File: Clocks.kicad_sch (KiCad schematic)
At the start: 9 parts, among them U3 CDCLVC1106, Y2 O 16,0-JT22CT-A-P-3,3-LF

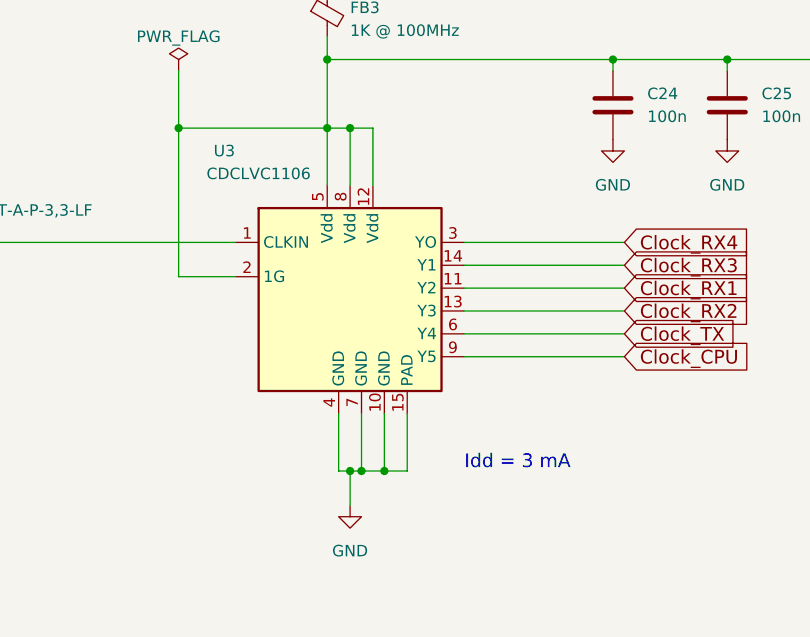
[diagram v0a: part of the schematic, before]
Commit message: Change the clock buffer
Move to one that is temperature rated and has better specs.

Also reroute one clock line to move it from board edge.

Get a list of all parts that aren't rated to at least 105C.

Signed-off-by: Corey Minyard <corey@minyard.net>
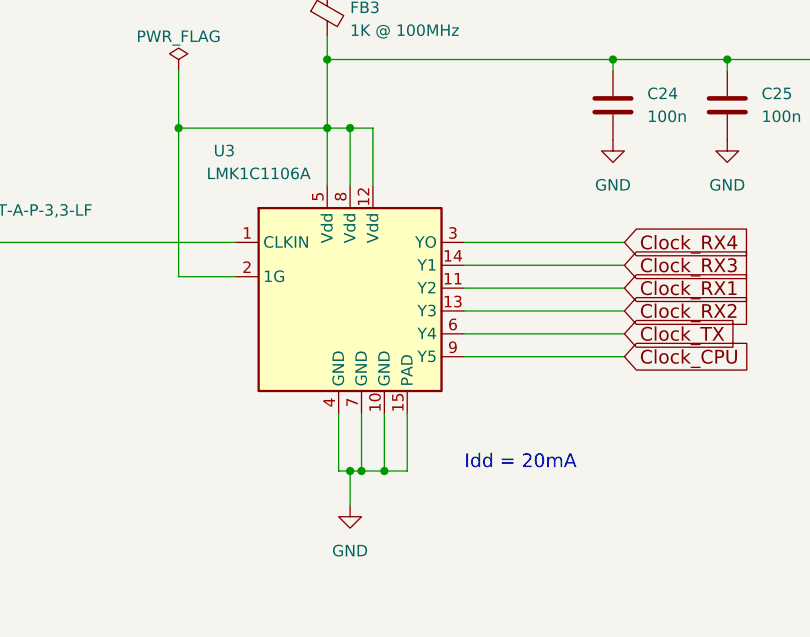
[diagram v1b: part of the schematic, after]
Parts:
- U3: value CDCLVC1106 -> LMK1C1106A; symbol PACSAT_ICs:CDCLVP1106 -> PACSAT_ICs:LMK1C1106A
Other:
- note added: "Idd = 20mA"
- note removed: "Idd = 3 mA"
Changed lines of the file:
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@@
 		)
 	)
-	(text "Idd = 3 mA"
+	(text "Idd = 20mA"
 		(exclude_from_sim no)
 		(at 228.6 132.08 0)
@@
 	)
 	(symbol
-		(lib_id "PACSAT_ICs:CDCLVP1106")
+		(lib_id "PACSAT_ICs:LMK1C1106A")
 		(at 215.9 113.03 0)
 		(unit 1)
@@
 			)
 		)
-		(property "Value" "CDCLVC1106"
+		(property "Value" "LMK1C1106A"
 			(at 205.74 99.06 0)
 			(effects
@@
 					(size 1.27 1.27)
 				)
-			)
-		)
+				(hide yes)
+			)
+		)

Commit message: More work on various things
Signed-off-by: Corey Minyard <corey@minyard.net>
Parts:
- added R56: 33, Resistor_SMD:R_0603_1608Metric_Pad0.98x0.95mm_HandSolder, symbol Device:R
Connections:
- net Clock_CPU: now also R56.2; no longer U3.9 (Y5)
- new net: R56.1, U3.9 (Y5)
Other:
- note added: "AX5043s have capacitive termination at the end of the clocks per their data sheet. Only need series termination on the CPU clock."
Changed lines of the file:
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@@
+		)
+	)
+	(text "AX5043s have capacitive termination\nat the end of the clocks per their\ndata sheet.  Only need series\ntermination on the CPU clock."
+		(exclude_from_sim no)
+		(at 248.412 134.874 0)
+		(effects
+			(font
+				(size 1.524 1.524)
+			)
 		)
 	)
@@
 	(text "Idd = 20mA"
 		(exclude_from_sim no)
-		(at 228.6 132.08 0)
+		(at 195.58 131.826 0)
 		(effects
 			(font
@@
 	(wire
 		(pts
+			(xy 233.68 119.38) (xy 228.6 119.38)
+		)
+		(stroke
+			(width 0)
+			(type default)
+		)
+	)
+	(wire
+		(pts
 			(xy 163.83 106.68) (xy 203.2 106.68)
 		)
@@
 	(wire
 		(pts
+			(xy 242.57 123.19) (xy 246.38 123.19)
+		)
+		(stroke
+			(width 0)
+			(type default)
+		)
+	)
+	(wire
+		(pts
 			(xy 228.6 106.68) (xy 246.38 106.68)
 		)
@@
 	(wire
 		(pts
-			(xy 228.6 119.38) (xy 246.38 119.38)
+			(xy 233.68 123.19) (xy 234.95 123.19)
 		)
 		(stroke
@@
 		(pts
 			(xy 203.2 110.49) (xy 196.85 110.49)
+		)
+		(stroke
+			(width 0)
+			(type default)
+		)
+	)
+	(wire
+		(pts
+			(xy 233.68 123.19) (xy 233.68 119.38)
 		)
 		(stroke
@@
 	(global_label "Clock_CPU"
 		(shape input)
-		(at 246.38 119.38 0)
+		(at 246.38 123.19 0)
 		(fields_autoplaced yes)
 		(effects
@@
 		)
 		(property "Intersheetrefs" "${INTERSHEET_REFS}"
-			(at 261.2237 119.38 0)
+			(at 261.2237 123.19 0)
 			(effects
 				(font
@@
 					(unit 1)
 				)
+			)
+		)
+	)
+	(symbol
+		(lib_id "Device:R")
+		(at 238.76 123.19 90)
+		(unit 1)
+		(exclude_from_sim no)
+		(in_bom yes)
+		(on_board yes)
+		(dnp no)
+		(property "Reference" "R56"
+			(at 241.3 125.73 90)
+			(effects
+				(font
+					(size 1.27 1.27)
+				)
+				(justify left)
+			)
+		)
+		(property "Value" "33"
+			(at 240.538 120.904 90)
+			(effects
+				(font
+					(size 1.27 1.27)
+				)
+				(justify left)
+			)
+		)
+		(property "Footprint" "Resistor_SMD:R_0603_1608Metric_Pad0.98x0.95mm_HandSolder"
+			(at 238.76 124.968 90)
+			(effects
+				(font
+					(size 1.27 1.27)
+				)
+				(hide yes)
+			)
+		)
+		(property "Datasheet" "~"
+			(at 238.76 123.19 0)
+			(effects
+				(font
+					(size 1.27 1.27)
+				)
+			)
+		)
+		(property "Description" ""
+			(at 238.76 123.19 0)
+			(effects
+				(font
+					(size 1.27 1.27)
+				)
+			)
+		)
+		(pin "1"
+		)
+		(pin "2"
+		)
+		(instances
+			(project "PacSat_AFSK"
+				(path "/cc9f42d2-6985-41ac-acab-5ab7b01c5b38/a735fef7-c3fa-4339-b3a6-fbce810c3c4b"
+					(reference "R56")
+					(unit 1)
+				)

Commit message: Change clock and MRAM passives to 0402
Signed-off-by: Corey Minyard <corey@minyard.net>
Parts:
- C23, C24, C25, C26: footprint Capacitor_SMD:C_0603_1608Metric_Pad1.08x0.95mm_HandSolder -> Capacitor_SMD:C_0402_1005Metric_Pad0.74x0.62mm_HandSolder
- R25, R56: footprint Resistor_SMD:R_0603_1608Metric_Pad0.98x0.95mm_HandSolder -> Resistor_SMD:R_0402_1005Metric_Pad0.72x0.64mm_HandSolder
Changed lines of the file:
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@@
 			)
 		)
-		(property "Footprint" "Capacitor_SMD:C_0603_1608Metric_Pad1.08x0.95mm_HandSolder"
+		(property "Footprint" "Capacitor_SMD:C_0402_1005Metric_Pad0.74x0.62mm_HandSolder"
 			(at 246.0752 95.25 0)
 			(effects
@@
 			)
 		)
-		(property "Footprint" "Resistor_SMD:R_0603_1608Metric_Pad0.98x0.95mm_HandSolder"
+		(property "Footprint" "Resistor_SMD:R_0402_1005Metric_Pad0.72x0.64mm_HandSolder"
 			(at 238.76 124.968 90)
 			(effects
@@
 			)
 		)
-		(property "Footprint" "Resistor_SMD:R_0603_1608Metric_Pad0.98x0.95mm_HandSolder"
+		(property "Footprint" "Resistor_SMD:R_0402_1005Metric_Pad0.72x0.64mm_HandSolder"
 			(at 137.922 100.33 90)
 			(effects
@@
 			)
 		)
-		(property "Footprint" "Capacitor_SMD:C_0603_1608Metric_Pad1.08x0.95mm_HandSolder"
+		(property "Footprint" "Capacitor_SMD:C_0402_1005Metric_Pad0.74x0.62mm_HandSolder"
 			(at 126.6952 111.76 0)
 			(effects
@@
 			)
 		)
-		(property "Footprint" "Capacitor_SMD:C_0603_1608Metric_Pad1.08x0.95mm_HandSolder"
+		(property "Footprint" "Capacitor_SMD:C_0402_1005Metric_Pad0.74x0.62mm_HandSolder"
 			(at 258.7752 95.25 0)
 			(effects
@@
 			)
 		)
-		(property "Footprint" "Capacitor_SMD:C_0603_1608Metric_Pad1.08x0.95mm_HandSolder"
+		(property "Footprint" "Capacitor_SMD:C_0402_1005Metric_Pad0.74x0.62mm_HandSolder"
 			(at 271.4752 95.25 0)
 			(effects

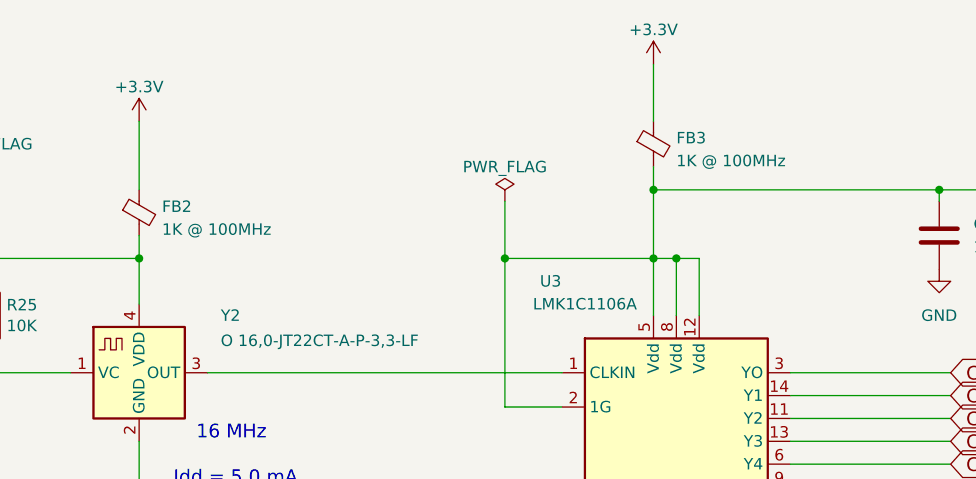
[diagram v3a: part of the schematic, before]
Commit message: More work on components
Signed-off-by: Corey Minyard <corey@minyard.net>
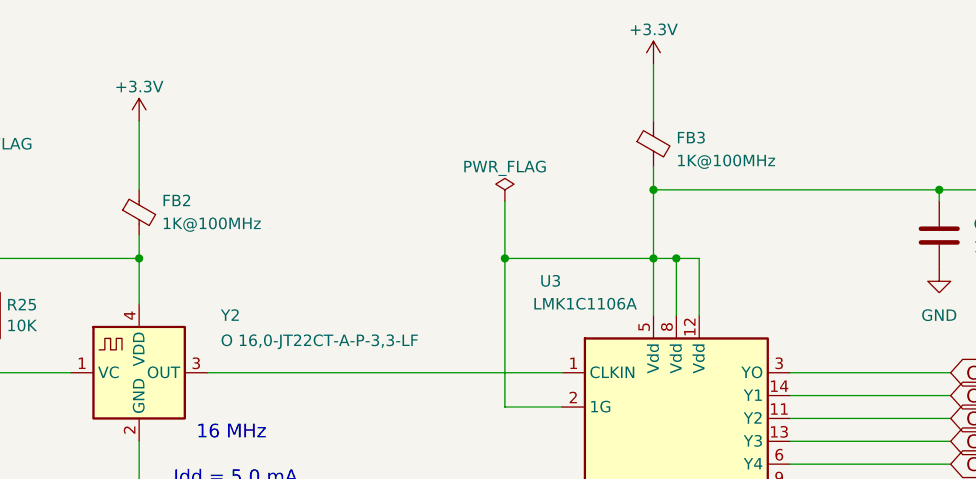
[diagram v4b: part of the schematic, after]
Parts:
- FB2, FB3: value 1K @ 100MHz -> 1K@100MHz
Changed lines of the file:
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@@
 		(fields_autoplaced yes)
 		(property "Reference" "FB2"
-			(at 158.75 88.2269 0)
-			(effects
-				(font
-					(size 1.27 1.27)
-				)
-				(justify left)
-			)
-		)
-		(property "Value" "1K @ 100MHz"
-			(at 158.75 90.7669 0)
+			(at 158.75 87.5918 0)
+			(effects
+				(font
+					(size 1.27 1.27)
+				)
+				(justify left)
+			)
+		)
+		(property "Value" "1K@100MHz"
+			(at 158.75 90.1318 0)
 			(effects
 				(font
@@
 			)
 		)
-		(property "Value" "1K @ 100MHz"
+		(property "Value" "1K@100MHz"
 			(at 215.9 83.1469 0)
 			(effects

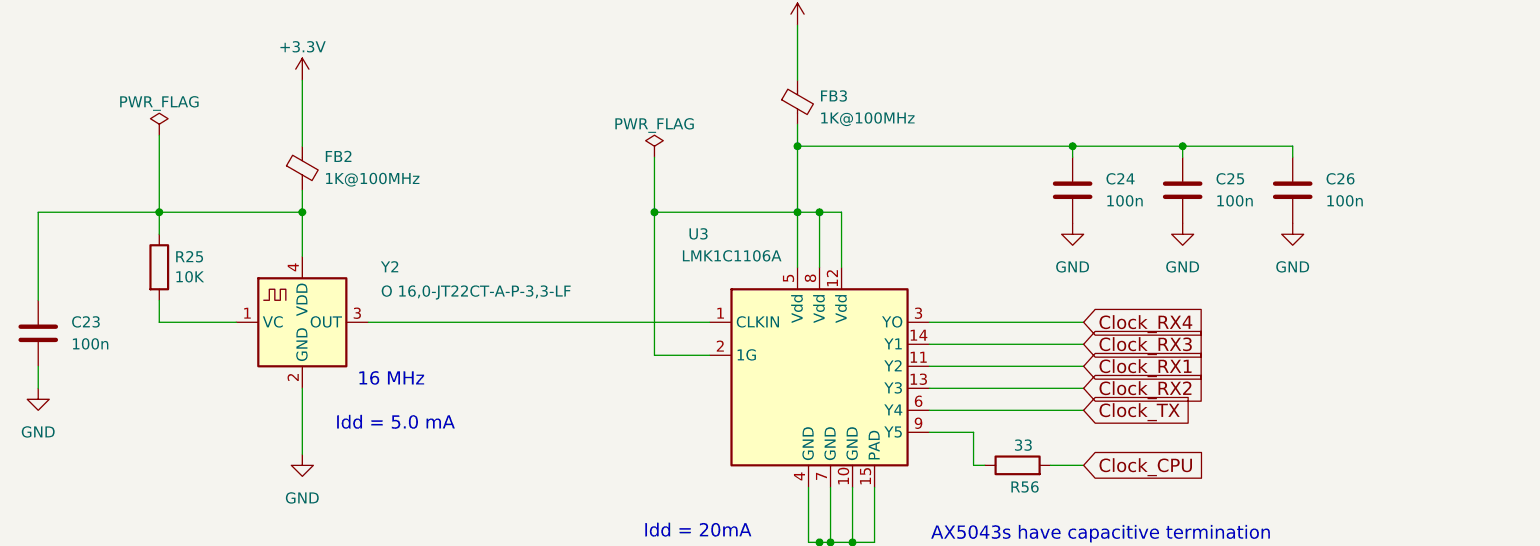
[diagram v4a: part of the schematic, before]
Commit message: Lots of updates to ease manufacturing
Component changes, changes in the formatting of the values, etc.

Signed-off-by: Corey Minyard <corey@minyard.net>
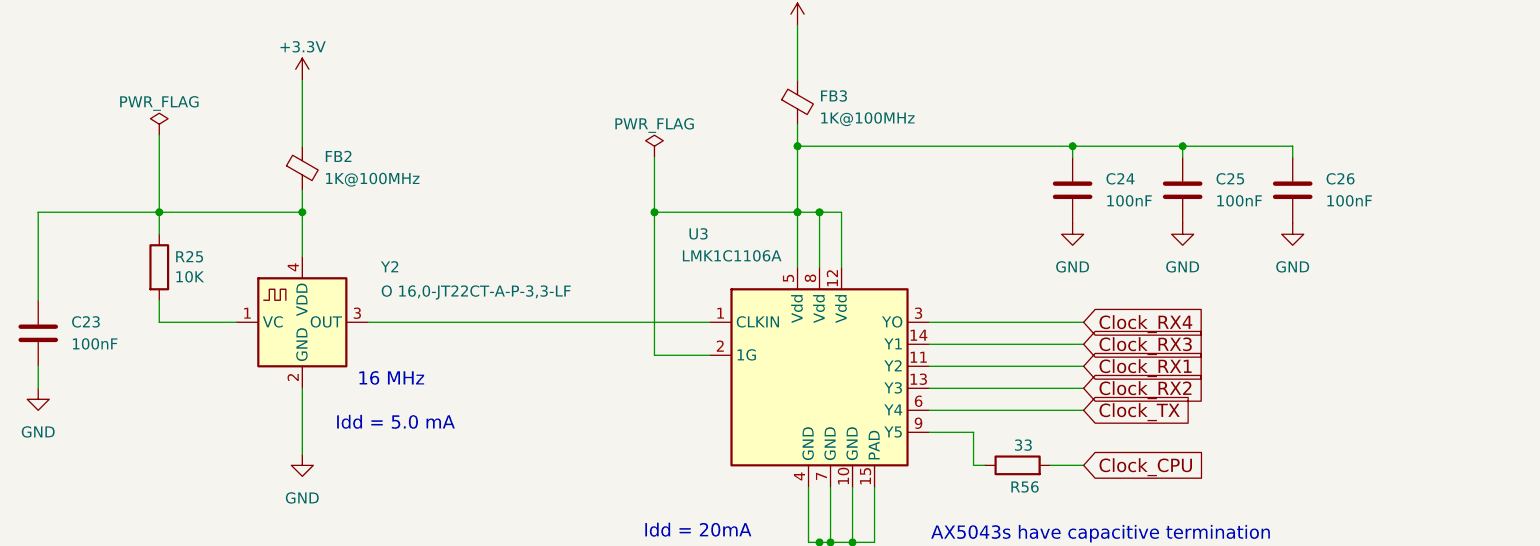
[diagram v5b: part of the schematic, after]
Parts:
- C23, C24, C25, C26: value 100n -> 100nF
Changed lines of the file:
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@@
 			)
 		)
-		(property "Value" "100n"
+		(property "Value" "100nF"
 			(at 248.92 92.7099 0)
 			(effects
@@
 			)
 		)
-		(property "Value" "100n"
+		(property "Value" "100nF"
 			(at 129.54 109.2199 0)
 			(effects
@@
 			)
 		)
-		(property "Value" "100n"
+		(property "Value" "100nF"
 			(at 261.62 92.7099 0)
 			(effects
@@
 			)
 		)
-		(property "Value" "100n"
+		(property "Value" "100nF"
 			(at 274.32 92.7099 0)
 			(effects

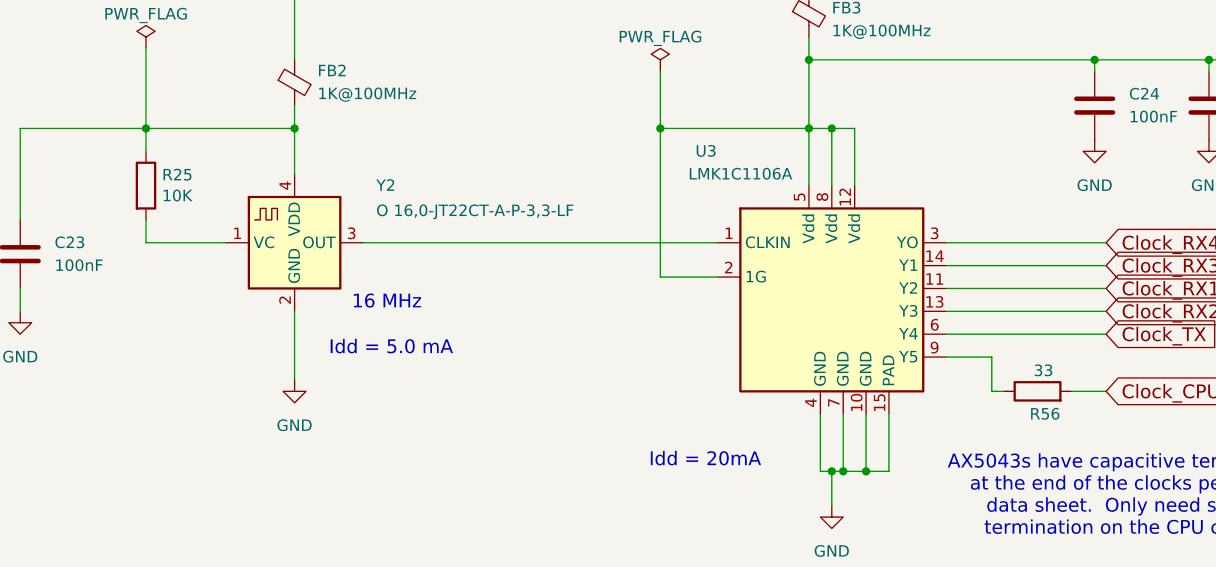
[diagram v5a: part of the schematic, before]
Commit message: Update all resistors to have an ohm symbol
Make it more clean in the BOM what they are.

Signed-off-by: Corey Minyard <corey@minyard.net>
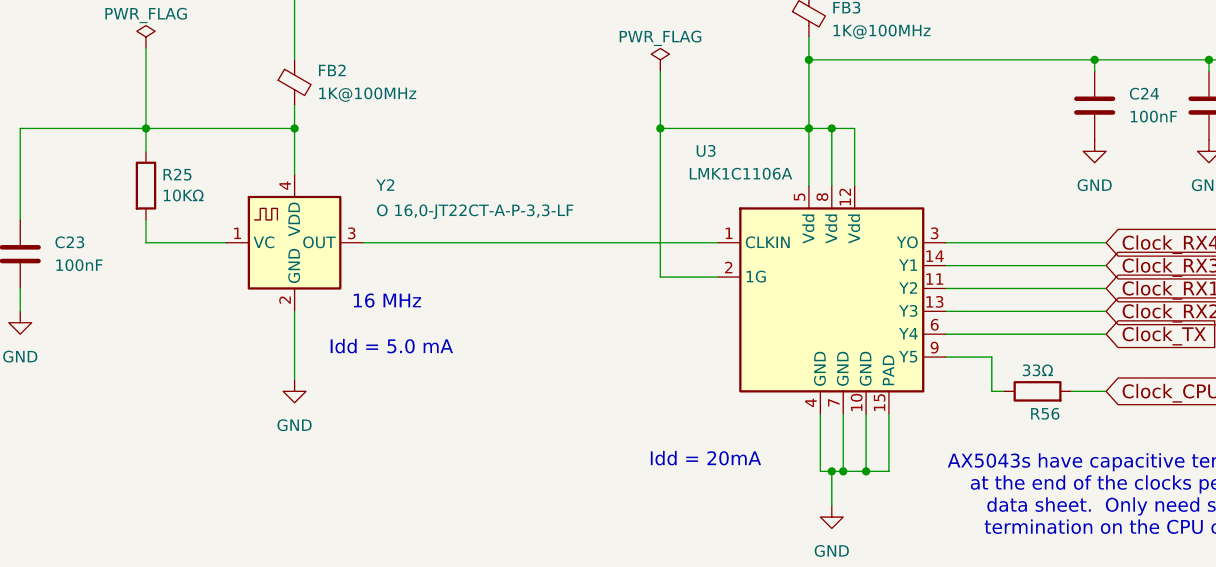
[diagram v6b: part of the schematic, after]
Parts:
- R25: value 10K -> 10KΩ
- R56: value 33 -> 33Ω
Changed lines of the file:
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@@
 			)
 		)
-		(property "Value" "33"
+		(property "Value" "33Ω"
 			(at 240.538 120.904 90)
 			(effects
@@
 			)
 		)
-		(property "Value" "10K"
+		(property "Value" "10KΩ"
 			(at 141.478 101.473 0)
 			(effects

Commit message: Have the BOM file fixer output xls, not csv
The omega symbol gets translated properly from xls.

Signed-off-by: Corey Minyard <corey@minyard.net>
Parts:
- FB2, FB3: footprint Resistor_SMD:R_0603_1608Metric_Pad0.98x0.95mm_HandSolder -> Inductor_SMD:L_0603_1608Metric_Pad1.05x0.95mm_HandSolder
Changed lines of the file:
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@@
 			)
 		)
-		(property "Footprint" "Resistor_SMD:R_0603_1608Metric_Pad0.98x0.95mm_HandSolder"
+		(property "Footprint" "Inductor_SMD:L_0603_1608Metric_Pad1.05x0.95mm_HandSolder"
 			(at 154.432 88.9 90)
 			(effects
@@
 			(project "PacSat_Dev_RevD_240614"
 				(path "/cc9f42d2-6985-41ac-acab-5ab7b01c5b38/a735fef7-c3fa-4339-b3a6-fbce810c3c4b"
+					(reference "FB2")
+					(unit 1)
+				)
+				(path "/cc9f42d2-6985-41ac-acab-5ab7b01c5b38/d9a83ee4-3280-49b9-88b8-54d26cbd8ed1/7fb6f4ad-3f2f-474c-8e36-07b875720381"
 					(reference "FB2")
 					(unit 1)
@@
 			)
 		)
-		(property "Footprint" "Resistor_SMD:R_0603_1608Metric_Pad0.98x0.95mm_HandSolder"
+		(property "Footprint" "Inductor_SMD:L_0603_1608Metric_Pad1.05x0.95mm_HandSolder"
 			(at 211.582 81.28 90)
 			(effects

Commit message: Minor fixes for BOM values
Signed-off-by: Corey Minyard <corey@minyard.net>
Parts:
- FB2, FB3: value 1K@100MHz -> 1KΩ@100MHz
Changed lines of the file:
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@@
 			)
 		)
-		(property "Value" "1K@100MHz"
+		(property "Value" "1KΩ@100MHz"
 			(at 158.75 90.1318 0)
 			(effects
@@
 			)
 		)
-		(property "Value" "1K@100MHz"
+		(property "Value" "1KΩ@100MHz"
 			(at 215.9 83.1469 0)
 			(effects
